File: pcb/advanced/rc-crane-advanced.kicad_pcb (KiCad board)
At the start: 2 copper layers, 100 x 100 mm, 72 parts, among them J10 DevKitC-1 J1, J11 DevKitC-1 J3, J12 DIAG0, J13 DIAG1, J14 DIAG2, J15 DIAG3, J20 Motor 0, J21 Motor 1, J22 Motor 2, J23 Motor 3, J30 PWM out, J4 RC in, J7 Serial RX, J8 I2C, J9 VM batt, U10 TMC2209 #0, U11 TMC2209 #1, U12 TMC2209 #2, U13 TMC2209 #3, U4 AMS1117-5.0, U5 PCA9685PW

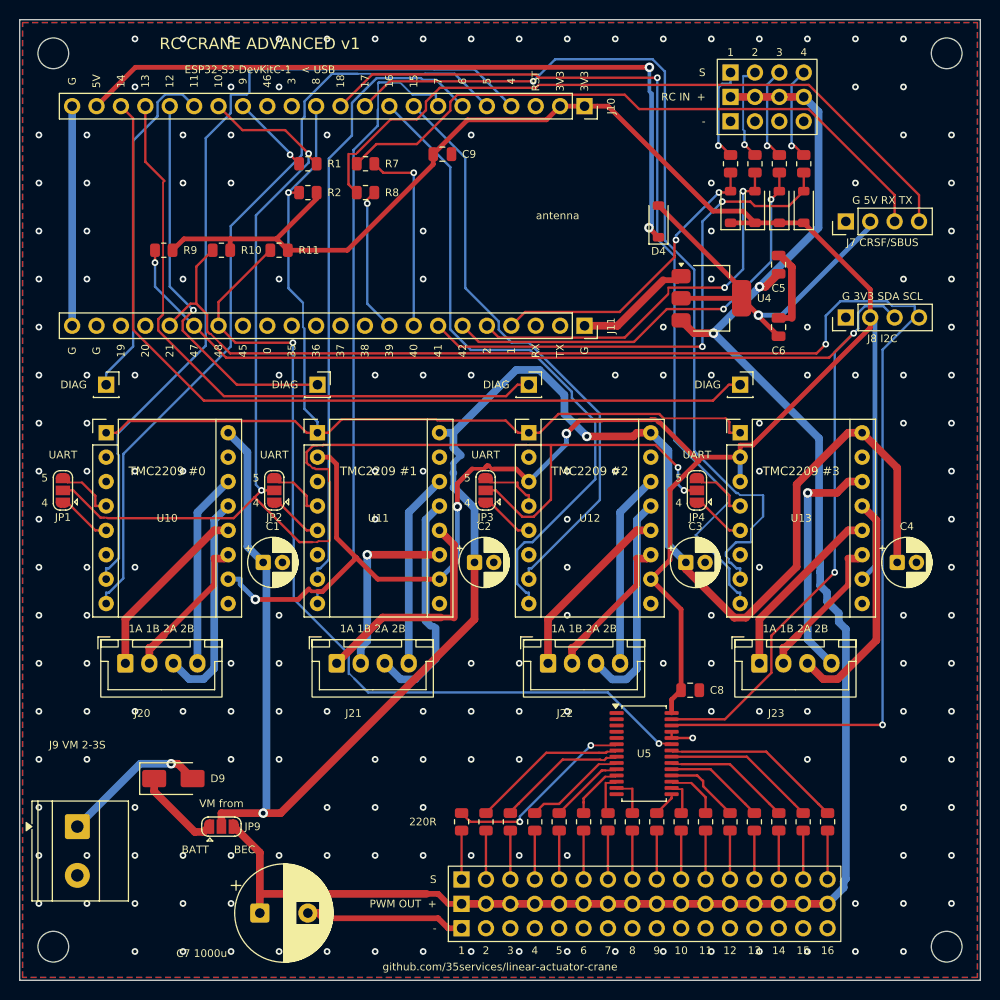
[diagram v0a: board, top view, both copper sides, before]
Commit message: Stacked version of the advanced board: two 84 x 76 mm boards
pcb/advanced-stack: top board (DevKitC-1, 4x TMC2209, motors; through-hole
only) and bottom board (PCA9685 + 16 outputs, RC/CRSF/I2C inputs, 5 V
regulator, VM input; JLCPCB SMD), joined by a 2x8 stacking header on
shared M3 holes. Bottom-board connectors are right-angle headers pointing
out of the edges so they stay reachable under the top board; the servo
buffer cap sits on the underside. Same nets as the single board.

board_tools: edge keepout border for the autorouter, island removal,
neck-downs only widened where the clearance allows (min. 0.125 mm),
right-angle header blocks, per-part 3D model overrides and bottom-side
parts. All boards: DRC 0 violations, 0 unconnected.

Co-Authored-By: Claude Opus 5.5 <noreply@anthropic.com>
Claude-Session: https://claude.ai/code/session_01JATcLE25KWRaki615r1Lis
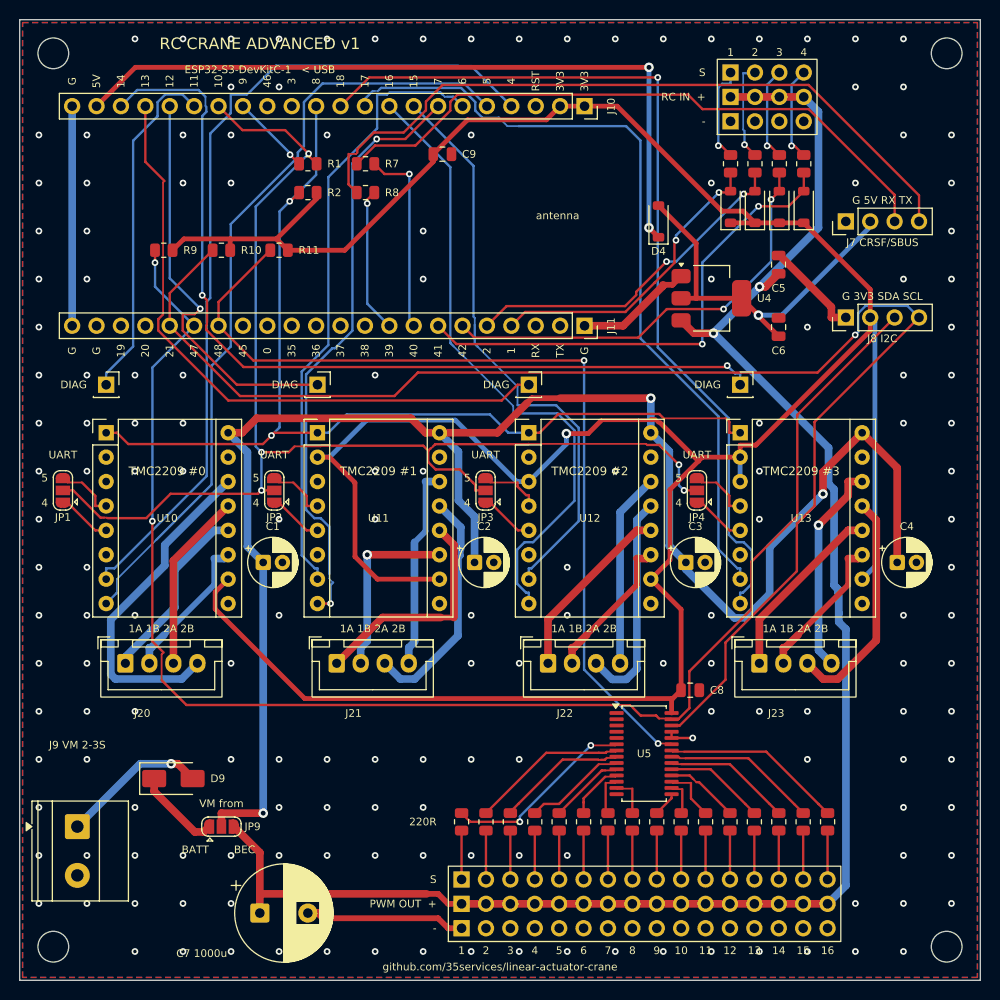
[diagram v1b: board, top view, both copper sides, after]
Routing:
- net +3V3: track 268.9 -> 314.1 mm, vias 3 -> 1
- net UART: track 154.1 -> 132.9 mm, vias 4 -> 5
- net SDA: track 138.8 -> 155.4 mm, vias 3 -> 2
- net VM: track 191.6 -> 175.6 mm, vias 2 -> 3
- net M0_2B: track 20.2 -> 35.0 mm
- net STEP3: track 95.8 -> 82.9 mm, vias 1 -> 0
- net SCL: track 159.6 -> 149.9 mm, vias 2 -> 1
- net RC1: track 41.8 -> 35.8 mm
- net M0_2A: track 22.9 -> 18.7 mm
- net RC3: track 55.6 -> 52.4 mm
- net M3_2B: track 24.9 -> 22.2 mm
- net DIR2: track 68.8 -> 66.1 mm
- net DIAG3: track 90.7 -> 93.2 mm, vias 0 -> 2
- net DIR1: track 64.8 -> 62.4 mm, vias 0 -> 2
- net PWM_OE: track 92.1 -> 94.1 mm
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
